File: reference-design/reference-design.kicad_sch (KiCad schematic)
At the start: 30 parts

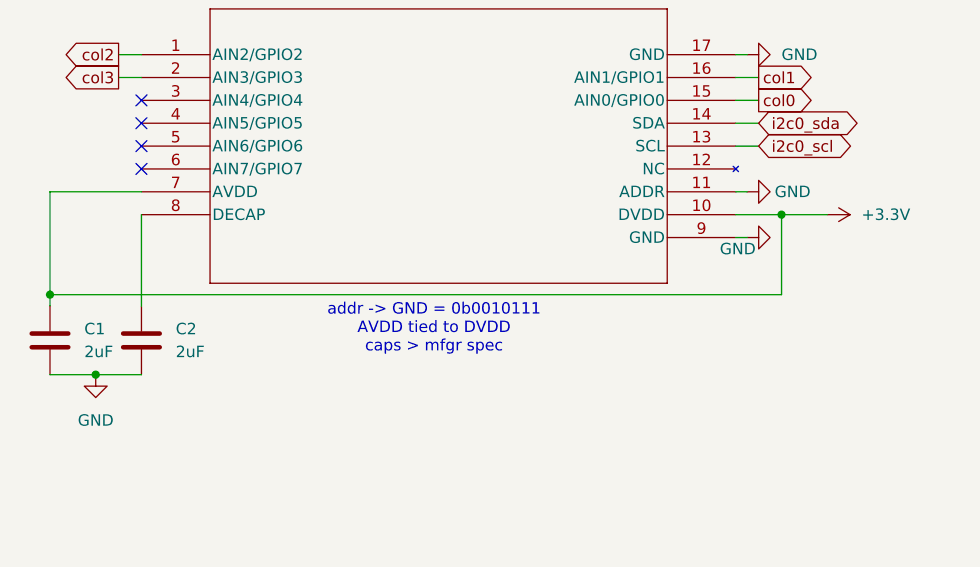
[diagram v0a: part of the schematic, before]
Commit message: fixes ADC ADDR being grounded in schematic
PCB still not updated, needs to be re-autorouted
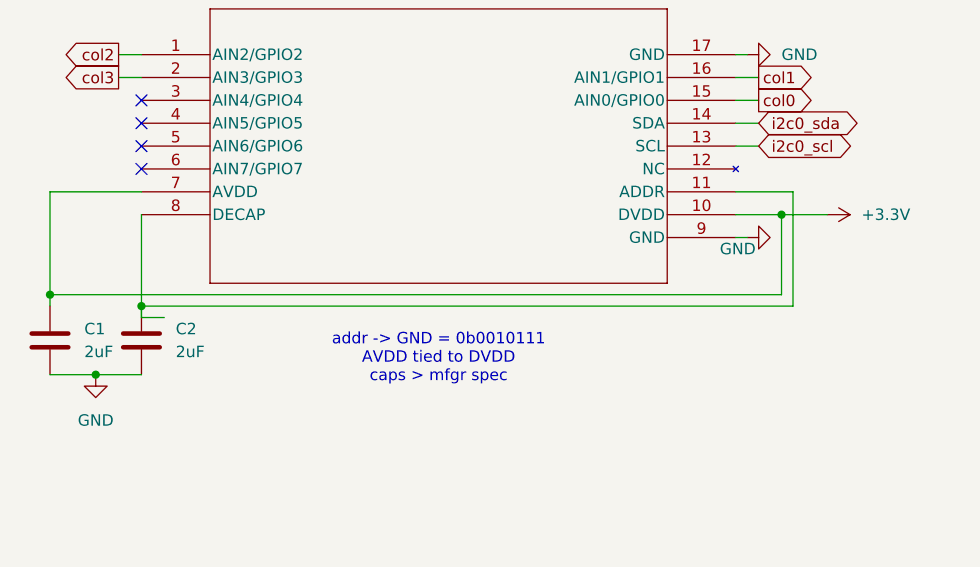
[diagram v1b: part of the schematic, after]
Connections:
- net GND: no longer ADC1.11 (ADDR)
- net at ADC1.8 (DECAP), C2.1: now also ADC1.11 (ADDR)
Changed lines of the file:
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@@
 	(text "addr -> GND = 0b0010111\nAVDD tied to DVDD\ncaps > mfgr spec"
 		(exclude_from_sim no)
-		(at 59.182 110.49 0)
+		(at 59.69 113.792 0)
 		(effects
 			(font
@@
 	)
 	(junction
+		(at 26.67 107.95)
+		(diameter 0)
+		(color 0 0 0 0)
+	)
+	(junction
 		(at 243.84 76.2)
 		(diameter 0)
@@
 	(wire
 		(pts
+			(xy 99.06 107.95) (xy 99.06 95.25)
+		)
+		(stroke
+			(width 0)
+			(type default)
+		)
+	)
+	(wire
+		(pts
 			(xy 243.84 104.14) (xy 215.9 104.14)
 		)
@@
 	(wire
 		(pts
+			(xy 26.67 109.22) (xy 26.67 107.95)
+		)
+		(stroke
+			(width 0)
+			(type default)
+		)
+	)
+	(wire
+		(pts
 			(xy 21.59 115.57) (xy 26.67 115.57)
 		)
@@
 	(wire
 		(pts
+			(xy 26.67 107.95) (xy 99.06 107.95)
+		)
+		(stroke
+			(width 0)
+			(type default)
+		)
+	)
+	(wire
+		(pts
 			(xy 60.96 185.42) (xy 63.5 185.42)
 		)
@@
 	(wire
 		(pts
-			(xy 93.98 95.25) (xy 92.71 95.25)
+			(xy 92.71 95.25) (xy 99.06 95.25)
+		)
+		(stroke
+			(width 0)
+			(type default)
+		)
+	)
+	(wire
+		(pts
+			(xy 29.21 109.22) (xy 26.67 109.22)
 		)
 		(stroke
@@
 					(unit 1)
 				)
-			)
-		)
-	)
-	(symbol
-		(lib_id "power:GND")
-		(at 93.98 95.25 90)
-		(unit 1)
-		(exclude_from_sim no)
-		(in_bom yes)
-		(on_board yes)
-		(dnp no)
-		(property "Reference" "#PWR026"
-			(at 100.33 95.25 0)
-			(effects
-				(font
-					(size 1.27 1.27)
-				)
-				(hide yes)
-			)
-		)
-		(property "Value" "GND"
-			(at 97.028 95.25 90)
-			(effects
-				(font
-					(size 1.27 1.27)
-				)
-				(justify right)
-			)
-		)
-		(property "Footprint" ""
-			(at 93.98 95.25 0)
-			(effects
-				(font
-					(size 1.27 1.27)
-				)
-				(hide yes)
-			)
-		)
-		(property "Datasheet" ""
-			(at 93.98 95.25 0)
-			(effects
-				(font
-					(size 1.27 1.27)
-				)
-				(hide yes)
-			)
-		)
-		(property "Description" "Power symbol creates a global label with name \"GND\" , ground"
-			(at 93.98 95.25 0)
-			(effects
-				(font
-					(size 1.27 1.27)
-				)
-				(hide yes)
-			)
-		)
-		(pin "1"
-		)
-		(instances
-			(project ""
-				(path "/1bb90a40-7122-4522-9655-ffb2519dec46"
-					(reference "#PWR026")
-					(unit 1)
-				)
